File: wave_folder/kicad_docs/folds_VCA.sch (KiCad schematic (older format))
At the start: 13 parts, among them U1 SSM2164, U2 TL072

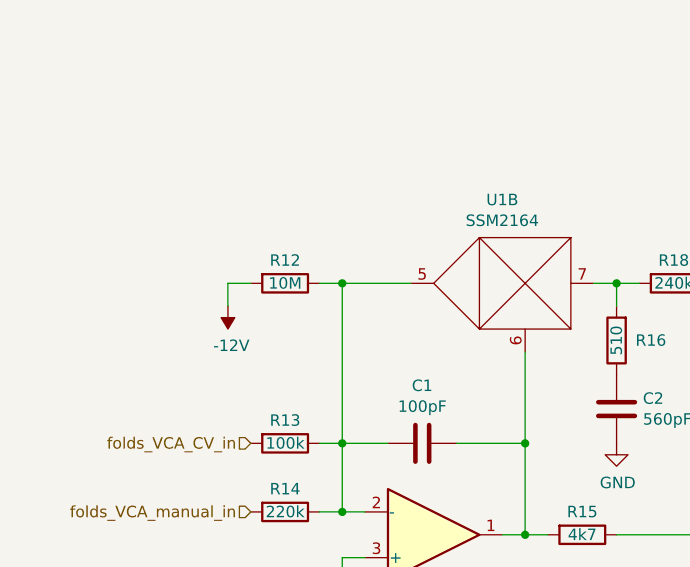
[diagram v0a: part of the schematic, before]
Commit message: small changes to wave folder CV bias and output level
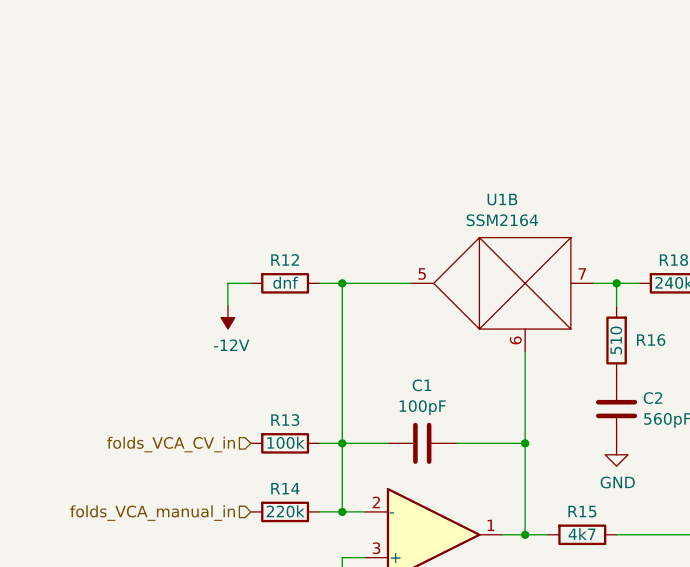
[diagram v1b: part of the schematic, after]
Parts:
- R12: value 10M -> dnf
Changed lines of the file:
@@
 P 3350 4700
 F 0 "R12" V 3250 4700 50  0000 C CNN
-F 1 "10M" V 3350 4700 50  0000 C CNN
+F 1 "dnf" V 3350 4700 50  0000 C CNN
 F 2 "Resistor_THT:R_Axial_DIN0207_L6.3mm_D2.5mm_P10.16mm_Horizontal" V 3280 4700 50  0001 C CNN
 F 3 "~" H 3350 4700 50  0001 C CNN
